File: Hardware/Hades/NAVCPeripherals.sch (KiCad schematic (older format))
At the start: 29 parts, among them U10 u-blox MAX-8Q, U5 BMI088, U6 TMP100, U7 MPRLS0025PA00001A, U8 IIS2MDCTR, U9 24CW1280T-I_OT

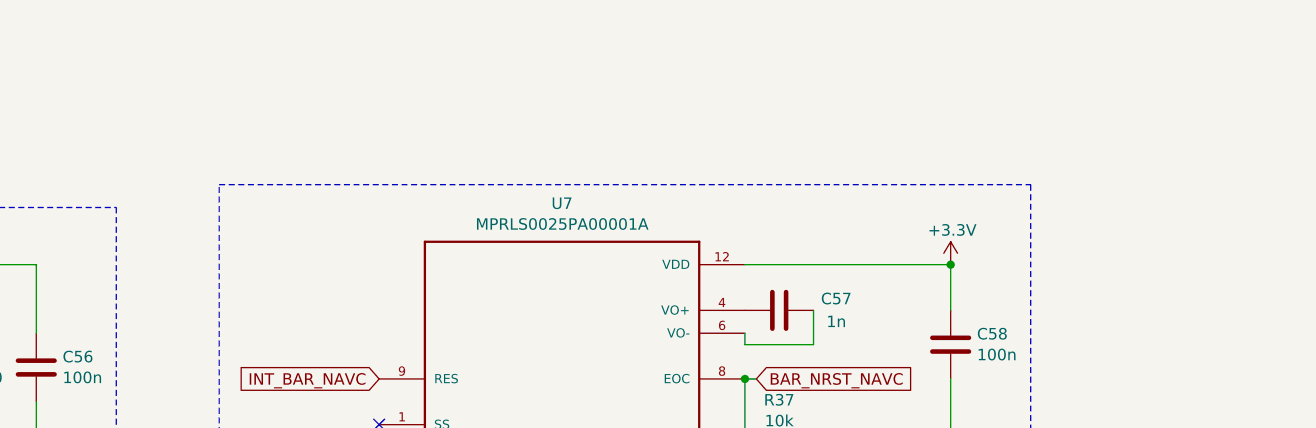
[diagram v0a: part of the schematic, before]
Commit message: Hardware arrived. Added drivers, tests, etc...
- Tested STM32F4 and STM32F7. Programmable via DFU.
- Barometer driver.
- Magnetometer driver.
- IMU driver.
- F4 25 MHz HSE seems to work.

Also created Hades Micro schematic. Need to finish PCB layout and routing.
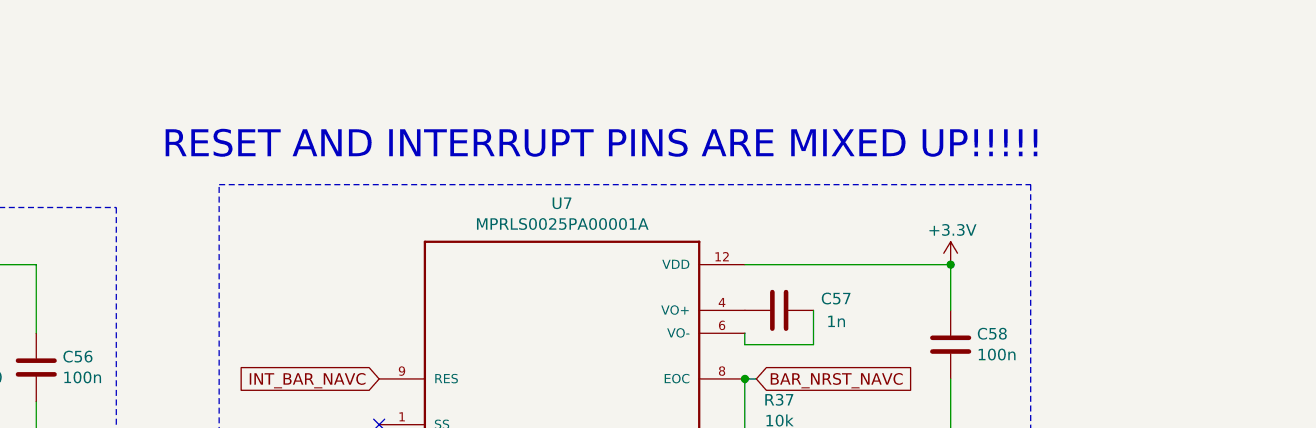
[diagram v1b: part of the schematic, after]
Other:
- note added: "RESET AND INTERRUPT PINS ARE MIXED UP!!!!!"
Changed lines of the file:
@@
 EESchema Schematic File Version 4
 LIBS:Hades-cache
-EELAYER 29 0
+EELAYER 26 0
 EELAYER END
 $Descr A4 11693 8268
@@
 	4250 6500 4550 6500
 Connection ~ 4550 6500
+Text Notes 7200 1100 0    118  ~ 0
+RESET AND INTERRUPT PINS ARE MIXED UP!!!!!
 $EndSCHEMATC
